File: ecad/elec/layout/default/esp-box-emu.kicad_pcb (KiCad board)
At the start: 2 copper layers, 225.7 x 100.8 mm, 25 parts

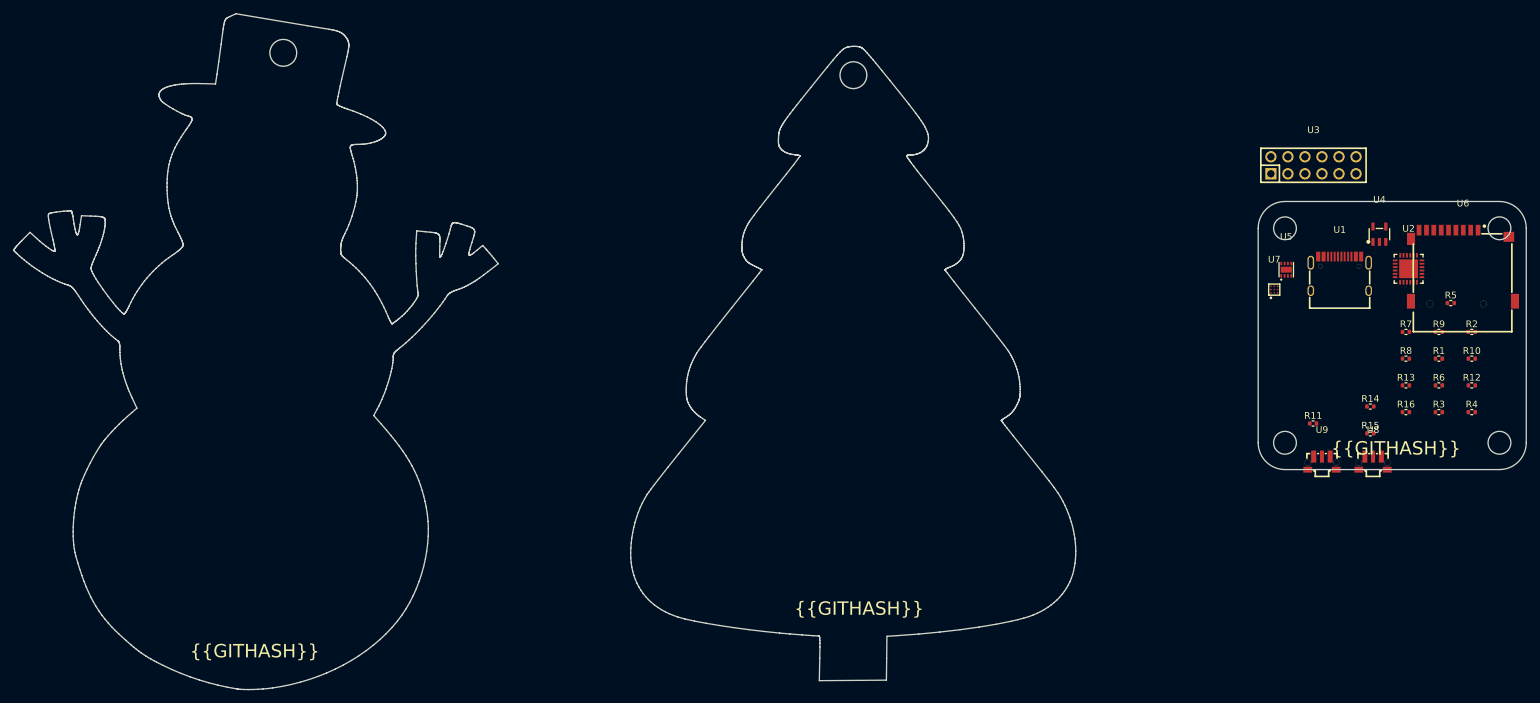
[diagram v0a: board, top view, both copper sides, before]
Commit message: playing with kicad layout for esp-box-emu board. added pmod headers
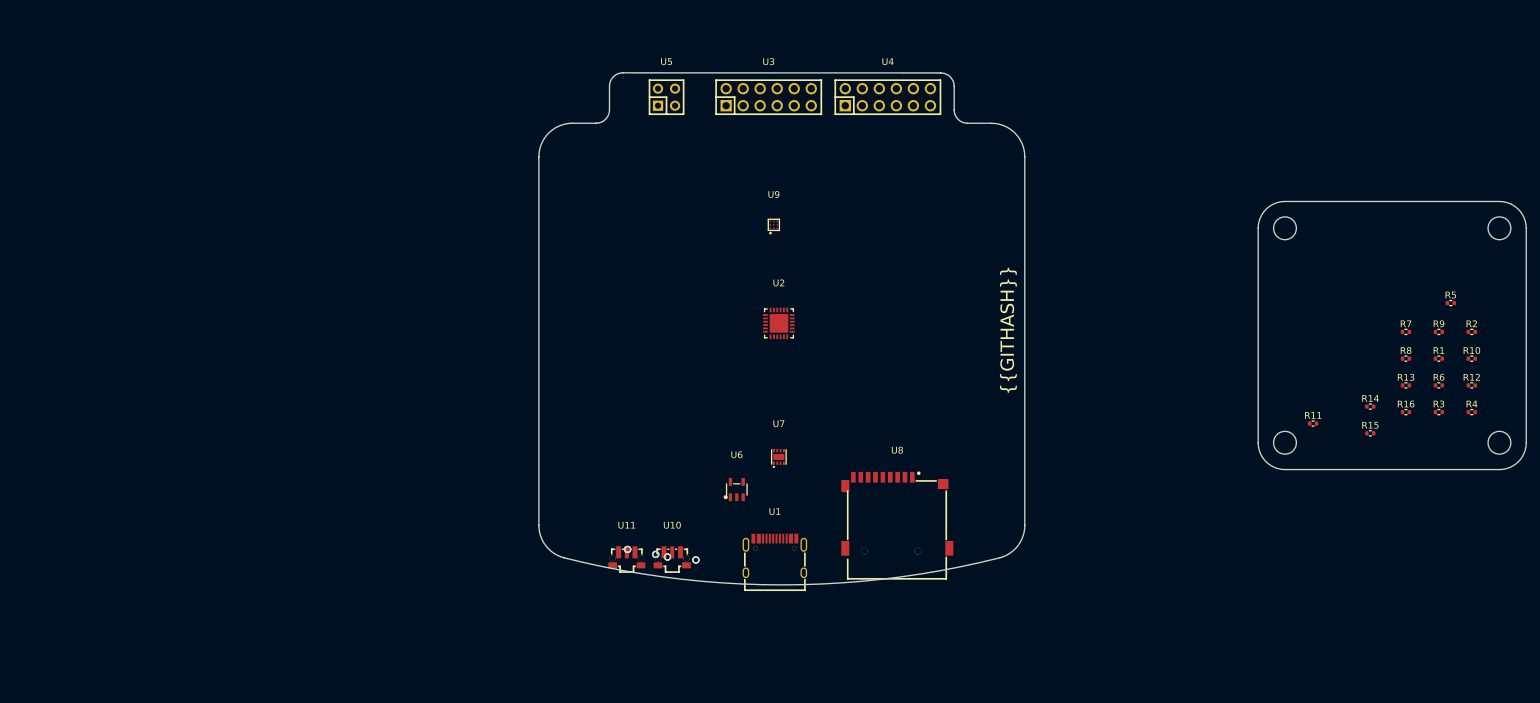
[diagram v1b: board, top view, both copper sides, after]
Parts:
- added U10: , lib:SW-SMD_E-SWITCH_TL3340, F.Cu at (134.2, 131.1)
- added U11: , lib:SW-SMD_E-SWITCH_TL3340, F.Cu at (127.4, 131.1)
- U4: footprint lib:SOT-23-5_L3.0-W1.7-P0.95-LS2.8-BL -> lib:HDR-TH_12P-P2.54-V-M-R2-C6-S2.54
- U5: footprint lib:DFN-8_L2.0-W2.0-P0.50-BL-EP -> lib:HDR-TH_4P-P2.54-V-M-R2-C2-S2.54-1
- U6: footprint lib:SIM-SMD_C9900007362 -> lib:SOT-23-5_L3.0-W1.7-P0.95-LS2.8-BL
- U7: footprint lib:DSBGA-9_L1.5-W1.5-R3-C3-P0.50-BL -> lib:DFN-8_L2.0-W2.0-P0.50-BL-EP
- U8: footprint lib:SW-SMD_E-SWITCH_TL3340 -> lib:SIM-SMD_C9900007362
- U9: footprint lib:SW-SMD_E-SWITCH_TL3340 -> lib:DSBGA-9_L1.5-W1.5-R3-C3-P0.50-BL
- moved U6 113.4 mm to (143.8, 120.8)
- moved U5 96.0 mm to (133.3, 62.2)
- moved U2 94.3 mm to (150.1, 96.0)
- moved U1 94.2 mm to (149.5, 130.6)
- moved U9 89.2 mm to (149.4, 81.3)
- moved U3 81.9 mm to (148.6, 62.2)
- moved U7 78.0 mm to (150.1, 115.9)
- moved U4 76.1 mm to (166.4, 62.2)
- moved U8 71.4 mm to (167.8, 124.2)
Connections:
- net _1 renamed pmod1-_1
- net _10 renamed pmod1-_10
- net _11 renamed pmod1-_11
- net _12 renamed pmod1-_12
- net _2 renamed pmod1-_2
- net _3 renamed pmod1-_3
- net _5 renamed pmod1-_5
- net _6 renamed pmod1-_6
- net _7 renamed pmod1-_7
- net _8 renamed pmod1-_8
- net _9 renamed pmod1-_9
- net mtp-_4 renamed pmod1-_4
- U4 pad 1: stat -> pmod2-_1
- U4 pad 2: gnd -> pmod2-_2
- U4 pad 3: vcc-2 -> pmod2-_3
- U4 pad 4: vcc-1 -> pmod2-_4
- U4 pad 5: gnd -> pmod2-_5
- U5 pad 1: ctg -> pin2x2-_1
- U5 pad 2: vcc-2 -> pin2x2-_2
- U5 pad 3: vcc-2 -> pin2x2-_3
- U5 pad 4: gnd -> pin2x2-_4
- U6 pad 1: dat2 -> stat
- U6 pad 2: cd_dat3 -> gnd
- U6 pad 3: cmd -> vcc-2
- U6 pad 4: vdd -> vcc-1
- U6 pad 5: clx -> gnd
- U8 pad 1: p1_2 -> dat2
- U8 pad 2: vcc -> cd_dat3
- U8 pad 3: vcc -> cmd
- U8 pad 4: vol_up.btn.btn-_4 -> vdd
- U8 pad 5: vol_up.btn.btn-_4 -> clx
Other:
- board size 225.7 x 100.8 mm -> 147.3 x 76.4 mm

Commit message: fleshing out more wiring and reworked pmod into separate module
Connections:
- net pmod2-_5 renamed _5
- net pmod2-_7 renamed _7
- U3 pad 10: pmod1-_10 -> gnd
- U3 pad 11: pmod1-_11 -> vcc
- U3 pad 12: pmod1-_12 -> vcc
- U3 pad 5: pmod1-_5 -> dm
- U3 pad 7: pmod1-_7 -> dp
- U3 pad 9: pmod1-_9 -> gnd
- U4 pad 10: pmod2-_10 -> gnd
- U4 pad 11: pmod2-_11 -> vcc
- U4 pad 12: pmod2-_12 -> vcc
- U4 pad 9: pmod2-_9 -> gnd
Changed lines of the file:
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@@
   (net 52 "pmod1-_3")
   (net 53 "pmod1-_4")
-  (net 54 "pmod1-_5")
-  (net 55 "pmod1-_6")
-  (net 56 "pmod1-_7")
-  (net 57 "pmod1-_8")
-  (net 58 "max17048-ep")
-  (net 59 "pin2x2-_1")
-  (net 60 "pin2x2-_2")
-  (net 61 "pin2x2-_3")
-  (net 62 "pin2x2-_4")
-  (net 63 "pmod1-_9")
-  (net 64 "pmod1-_10")
-  (net 65 "pmod1-_11")
-  (net 66 "pmod1-_12")
-  (net 67 "pmod2-_1")
-  (net 68 "pmod2-_2")
-  (net 69 "pmod2-_3")
-  (net 70 "pmod2-_4")
-  (net 71 "pmod2-_5")
-  (net 72 "pmod2-_6")
-  (net 73 "pmod2-_7")
-  (net 74 "pmod2-_8")
-  (net 75 "pmod2-_9")
-  (net 76 "pmod2-_10")
-  (net 77 "pmod2-_11")
-  (net 78 "pmod2-_12")
+  (net 54 "pmod1-_6")
+  (net 55 "pmod1-_8")
+  (net 56 "max17048-ep")
+  (net 57 "pin2x2-_1")
+  (net 58 "pin2x2-_2")
+  (net 59 "pin2x2-_3")
+  (net 60 "pin2x2-_4")
+  (net 61 "pmod2-_1")
+  (net 62 "pmod2-_2")
+  (net 63 "pmod2-_3")
+  (net 64 "pmod2-_4")
+  (net 65 "pmod2-_6")
+  (net 66 "pmod2-_8")
+  (net 67 "_5")
+  (net 68 "_7")
   (footprint "lib:SIM-SMD_C9900007362" (layer "F.Cu")
     (at 167.78 124.24)
@@
       (net 53 "pmod1-_4") (pintype "stereo"))
     (pad "5" thru_hole circle (at -1.27 1.27) (size 1.7 1.7) (drill 1.100023) (layers "*.Cu" "*.Mask")
-      (net 54 "pmod1-_5") (pintype "stereo"))
+      (net 27 "dm") (pintype "stereo"))
     (pad "6" thru_hole circle (at -1.27 -1.27) (size 1.7 1.7) (drill 1.100023) (layers "*.Cu" "*.Mask")
-      (net 55 "pmod1-_6") (pintype "stereo"))
+      (net 54 "pmod1-_6") (pintype "stereo"))
     (pad "7" thru_hole circle (at 1.27 1.27) (size 1.7 1.7) (drill 1.100023) (layers "*.Cu" "*.Mask")
-      (net 56 "pmod1-_7") (pintype "stereo"))
+      (net 28 "dp") (pintype "stereo"))
     (pad "8" thru_hole circle (at 1.27 -1.27) (size 1.7 1.7) (drill 1.100023) (layers "*.Cu" "*.Mask")
-      (net 57 "pmod1-_8") (pintype "stereo"))
+      (net 55 "pmod1-_8") (pintype "stereo"))
     (pad "9" thru_hole circle (at 3.81 1.27) (size 1.7 1.7) (drill 1.100023) (layers "*.Cu" "*.Mask")
-      (net 63 "pmod1-_9") (pintype "stereo"))
+      (net 9 "gnd") (pintype "stereo"))
     (pad "10" thru_hole circle (at 3.81 -1.27) (size 1.7 1.7) (drill 1.100023) (layers "*.Cu" "*.Mask")
-      (net 64 "pmod1-_10") (pintype "stereo"))
+      (net 9 "gnd") (pintype "stereo"))
     (pad "11" thru_hole circle (at 6.35 1.27) (size 1.7 1.7) (drill 1.100023) (layers "*.Cu" "*.Mask")
-      (net 65 "pmod1-_11") (pintype "stereo"))
+      (net 21 "vcc") (pintype "stereo"))
     (pad "12" thru_hole circle (at 6.35 -1.27) (size 1.7 1.7) (drill 1.100023) (layers "*.Cu" "*.Mask")
-      (net 66 "pmod1-_12") (pintype "stereo"))
+      (net 21 "vcc") (pintype "stereo"))
     (model "/Users/bob/esp-cpp/esp-box-emu/ecad/elec/footprints/footprints.3dshapes/HDR2.54-M-LI-2X6P.wrl"
       (offset (xyz 0 -0 0))
@@
       (stroke (width 0.06) (type solid)) (fill none) (layer "F.Fab"))
     (pad "1" thru_hole rect (at -6.35 1.27) (size 1.7 1.7) (drill 1.100023) (layers "*.Cu" "*.Mask")
-      (net 67 "pmod2-_1") (pintype "stereo"))
+      (net 61 "pmod2-_1") (pintype "stereo"))
     (pad "2" thru_hole circle (at -6.35 -1.27) (size 1.7 1.7) (drill 1.100023) (layers "*.Cu" "*.Mask")
-      (net 68 "pmod2-_2") (pintype "stereo"))
+      (net 62 "pmod2-_2") (pintype "stereo"))
     (pad "3" thru_hole circle (at -3.81 1.27) (size 1.7 1.7) (drill 1.100023) (layers "*.Cu" "*.Mask")
-      (net 69 "pmod2-_3") (pintype "stereo"))
+      (net 63 "pmod2-_3") (pintype "stereo"))
     (pad "4" thru_hole circle (at -3.81 -1.27) (size 1.7 1.7) (drill 1.100023) (layers "*.Cu" "*.Mask")
-      (net 70 "pmod2-_4") (pintype "stereo"))
+      (net 64 "pmod2-_4") (pintype "stereo"))
     (pad "5" thru_hole circle (at -1.27 1.27) (size 1.7 1.7) (drill 1.100023) (layers "*.Cu" "*.Mask")
-      (net 71 "pmod2-_5") (pintype "stereo"))
+      (net 67 "_5") (pintype "stereo"))
     (pad "6" thru_hole circle (at -1.27 -1.27) (size 1.7 1.7) (drill 1.100023) (layers "*.Cu" "*.Mask")
-      (net 72 "pmod2-_6") (pintype "stereo"))
+      (net 65 "pmod2-_6") (pintype "stereo"))
     (pad "7" thru_hole circle (at 1.27 1.27) (size 1.7 1.7) (drill 1.100023) (layers "*.Cu" "*.Mask")
-      (net 73 "pmod2-_7") (pintype "stereo"))
+      (net 68 "_7") (pintype "stereo"))
     (pad "8" thru_hole circle (at 1.27 -1.27) (size 1.7 1.7) (drill 1.100023) (layers "*.Cu" "*.Mask")
-      (net 74 "pmod2-_8") (pintype "stereo"))
+      (net 66 "pmod2-_8") (pintype "stereo"))
     (pad "9" thru_hole circle (at 3.81 1.27) (size 1.7 1.7) (drill 1.100023) (layers "*.Cu" "*.Mask")
-      (net 75 "pmod2-_9") (pintype "stereo"))
+      (net 9 "gnd") (pintype "stereo"))
     (pad "10" thru_hole circle (at 3.81 -1.27) (size 1.7 1.7) (drill 1.100023) (layers "*.Cu" "*.Mask")
-      (net 76 "pmod2-_10") (pintype "stereo"))
+      (net 9 "gnd") (pintype "stereo"))
     (pad "11" thru_hole circle (at 6.35 1.27) (size 1.7 1.7) (drill 1.100023) (layers "*.Cu" "*.Mask")
-      (net 77 "pmod2-_11") (pintype "stereo"))
+      (net 21 "vcc") (pintype "stereo"))
     (pad "12" thru_hole circle (at 6.35 -1.27) (size 1.7 1.7) (drill 1.100023) (layers "*.Cu" "*.Mask")
-      (net 78 "pmod2-_12") (pintype "stereo"))
+      (net 21 "vcc") (pintype "stereo"))
     (model "/Users/bob/esp-cpp/esp-box-emu/ecad/elec/footprints/footprints.3dshapes/HDR2.54-M-LI-2X6P.wrl"
       (offset (xyz 0 -0 0))
@@
       (net 20 "sda") (pintype "stereo"))
     (pad "9" smd rect (at 0 0) (size 1.65 0.9) (layers "F.Cu" "F.Paste" "F.Mask")
-      (net 58 "max17048-ep") (pintype "stereo"))
+      (net 56 "max17048-ep") (pintype "stereo"))
     (model "/Users/bob/esp-cpp/esp-box-emu/ecad/elec/footprints/footprints.3dshapes/DFN-8_L2.0-W2.0-H0.8-P0.50.wrl"
       (offset (xyz 0 -0 -0))
@@
       (stroke (width 0.06) (type solid)) (fill none) (layer "F.Fab"))
     (pad "1" thru_hole rect (at -1.27 1.27) (size 1.52 1.52) (drill 0.9144) (layers "*.Cu" "*.Mask")
-      (net 59 "pin2x2-_1") (pintype "stereo"))
+      (net 57 "pin2x2-_1") (pintype "stereo"))
     (pad "2" thru_hole circle (at -1.27 -1.27) (size 1.52 1.52) (drill 0.9144) (layers "*.Cu" "*.Mask")
-      (net 60 "pin2x2-_2") (pintype "stereo"))
+      (net 58 "pin2x2-_2") (pintype "stereo"))
     (pad "3" thru_hole circle (at 1.27 1.27) (size 1.52 1.52) (drill 0.9144) (layers "*.Cu" "*.Mask")
-      (net 61 "pin2x2-_3") (pintype "stereo"))
+      (net 59 "pin2x2-_3") (pintype "stereo"))
     (pad "4" thru_hole circle (at 1.27 -1.27) (size 1.52 1.52) (drill 0.9144) (layers "*.Cu" "*.Mask")
-      (net 62 "pin2x2-_4") (pintype "stereo"))
+      (net 60 "pin2x2-_4") (pintype "stereo"))
     (model "/Users/bob/esp-cpp/esp-box-emu/ecad/elec/footprints/footprints.3dshapes/HDR2.54-M-LI-2x2P.wrl"
       (offset (xyz 0 -0 0))

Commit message: fleshing out uSD card
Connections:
- net cd_dat3 renamed dat3
- net clx renamed clk
- net uSD-ep renamed uSD.card-ep
- U8 pad 4: vdd -> vcc
- U8 pad 6: vss -> gnd
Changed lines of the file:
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@@
   (net 39 "sbu1")
   (net 40 "dat2")
-  (net 41 "cd_dat3")
-  (net 42 "cmd")
-  (net 43 "vdd")
-  (net 44 "clx")
-  (net 45 "vss")
-  (net 46 "dat0")
-  (net 47 "dat1")
-  (net 48 "net")
-  (net 49 "uSD-ep")
-  (net 50 "pmod1-_1")
-  (net 51 "pmod1-_2")
-  (net 52 "pmod1-_3")
-  (net 53 "pmod1-_4")
-  (net 54 "pmod1-_6")
-  (net 55 "pmod1-_8")
-  (net 56 "max17048-ep")
-  (net 57 "pin2x2-_1")
-  (net 58 "pin2x2-_2")
-  (net 59 "pin2x2-_3")
-  (net 60 "pin2x2-_4")
-  (net 61 "pmod2-_1")
-  (net 62 "pmod2-_2")
-  (net 63 "pmod2-_3")
-  (net 64 "pmod2-_4")
-  (net 65 "pmod2-_6")
-  (net 66 "pmod2-_8")
-  (net 67 "_5")
-  (net 68 "_7")
+  (net 41 "cmd")
+  (net 42 "dat0")
+  (net 43 "dat1")
+  (net 44 "net")
+  (net 45 "pmod1-_1")
+  (net 46 "pmod1-_2")
+  (net 47 "pmod1-_3")
+  (net 48 "pmod1-_4")
+  (net 49 "pmod1-_6")
+  (net 50 "pmod1-_8")
+  (net 51 "max17048-ep")
+  (net 52 "pin2x2-_1")
+  (net 53 "pin2x2-_2")
+  (net 54 "pin2x2-_3")
+  (net 55 "pin2x2-_4")
+  (net 56 "pmod2-_1")
+  (net 57 "pmod2-_2")
+  (net 58 "pmod2-_3")
+  (net 59 "pmod2-_4")
+  (net 60 "pmod2-_6")
+  (net 61 "pmod2-_8")
+  (net 62 "_5")
+  (net 63 "_7")
+  (net 64 "dat3")
+  (net 65 "clk")
+  (net 66 "uSD.card-ep")
   (footprint "lib:SIM-SMD_C9900007362" (layer "F.Cu")
     (at 167.78 124.24)
@@
       (net 40 "dat2") (pintype "stereo"))
     (pad "2" smd rect (at 1.15 -5.3) (size 0.7 1.6) (layers "F.Cu" "F.Paste" "F.Mask")
-      (net 41 "cd_dat3") (pintype "stereo"))
+      (net 64 "dat3") (pintype "stereo"))
     (pad "3" smd rect (at 0.05 -5.3) (size 0.7 1.6) (layers "F.Cu" "F.Paste" "F.Mask")
-      (net 42 "cmd") (pintype "stereo"))
+      (net 41 "cmd") (pintype "stereo"))
     (pad "4" smd rect (at -1.05 -5.3) (size 0.7 1.6) (layers "F.Cu" "F.Paste" "F.Mask")
-      (net 43 "vdd") (pintype "stereo"))
+      (net 21 "vcc") (pintype "stereo"))
     (pad "5" smd rect (at -2.15 -5.3) (size 0.7 1.6) (layers "F.Cu" "F.Paste" "F.Mask")
-      (net 44 "clx") (pintype "stereo"))
+      (net 65 "clk") (pintype "stereo"))
     (pad "6" smd rect (at -3.25 -5.3) (size 0.7 1.6) (layers "F.Cu" "F.Paste" "F.Mask")
-      (net 45 "vss") (pintype "stereo"))
+      (net 9 "gnd") (pintype "stereo"))
     (pad "7" smd rect (at -4.35 -5.3) (size 0.7 1.6) (layers "F.Cu" "F.Paste" "F.Mask")
-      (net 46 "dat0") (pintype "stereo"))
+      (net 42 "dat0") (pintype "stereo"))
     (pad "8" smd rect (at -5.45 -5.3) (size 0.7 1.6) (layers "F.Cu" "F.Paste" "F.Mask")
-      (net 47 "dat1") (pintype "stereo"))
+      (net 43 "dat1") (pintype "stereo"))
     (pad "CD" smd rect (at -6.55 -5.3) (size 0.7 1.6) (layers "F.Cu" "F.Paste" "F.Mask")
-      (net 48 "net") (pintype "stereo"))
+      (net 44 "net") (pintype "stereo"))
     (pad "G" smd rect (at -7.76 5.3) (size 1.2 2.2) (layers "F.Cu" "F.Paste" "F.Mask")
-      (net 49 "uSD-ep") (pintype "stereo"))
+      (net 66 "uSD.card-ep") (pintype "stereo"))
     (pad "G" smd rect (at -7.75 -3.99) (size 1.2 1.8) (layers "F.Cu" "F.Paste" "F.Mask")
-      (net 49 "uSD-ep") (pintype "stereo"))
+      (net 66 "uSD.card-ep") (pintype "stereo"))
     (pad "G" smd rect (at 6.85 -4.29) (size 1.6 1.5) (layers "F.Cu" "F.Paste" "F.Mask")
-      (net 49 "uSD-ep") (pintype "stereo"))
+      (net 66 "uSD.card-ep") (pintype "stereo"))
     (pad "G" smd rect (at 7.76 5.3) (size 1.2 2.2) (layers "F.Cu" "F.Paste" "F.Mask")
-      (net 49 "uSD-ep") (pintype "stereo"))
+      (net 66 "uSD.card-ep") (pintype "stereo"))
     (model "/Users/bob/esp-cpp/esp-box-emu/ecad/elec/footprints/footprints.3dshapes/SIM-SMD_C9900007362.wrl"
       (offset (xyz -0 -2.19 0.5))
@@
       (stroke (width 0.06) (type solid)) (fill none) (layer "F.Fab"))
     (pad "1" thru_hole rect (at -6.35 1.27) (size 1.7 1.7) (drill 1.100023) (layers "*.Cu" "*.Mask")
-      (net 50 "pmod1-_1") (pintype "stereo"))
+      (net 45 "pmod1-_1") (pintype "stereo"))
     (pad "2" thru_hole circle (at -6.35 -1.27) (size 1.7 1.7) (drill 1.100023) (layers "*.Cu" "*.Mask")
-      (net 51 "pmod1-_2") (pintype "stereo"))
+      (net 46 "pmod1-_2") (pintype "stereo"))
     (pad "3" thru_hole circle (at -3.81 1.27) (size 1.7 1.7) (drill 1.100023) (layers "*.Cu" "*.Mask")
-      (net 52 "pmod1-_3") (pintype "stereo"))
+      (net 47 "pmod1-_3") (pintype "stereo"))
     (pad "4" thru_hole circle (at -3.81 -1.27) (size 1.7 1.7) (drill 1.100023) (layers "*.Cu" "*.Mask")
-      (net 53 "pmod1-_4") (pintype "stereo"))
+      (net 48 "pmod1-_4") (pintype "stereo"))
     (pad "5" thru_hole circle (at -1.27 1.27) (size 1.7 1.7) (drill 1.100023) (layers "*.Cu" "*.Mask")
       (net 27 "dm") (pintype "stereo"))
     (pad "6" thru_hole circle (at -1.27 -1.27) (size 1.7 1.7) (drill 1.100023) (layers "*.Cu" "*.Mask")
-      (net 54 "pmod1-_6") (pintype "stereo"))
+      (net 49 "pmod1-_6") (pintype "stereo"))
     (pad "7" thru_hole circle (at 1.27 1.27) (size 1.7 1.7) (drill 1.100023) (layers "*.Cu" "*.Mask")
       (net 28 "dp") (pintype "stereo"))
     (pad "8" thru_hole circle (at 1.27 -1.27) (size 1.7 1.7) (drill 1.100023) (layers "*.Cu" "*.Mask")
-      (net 55 "pmod1-_8") (pintype "stereo"))
+      (net 50 "pmod1-_8") (pintype "stereo"))
     (pad "9" thru_hole circle (at 3.81 1.27) (size 1.7 1.7) (drill 1.100023) (layers "*.Cu" "*.Mask")
       (net 9 "gnd") (pintype "stereo"))
@@
       (stroke (width 0.06) (type solid)) (fill none) (layer "F.Fab"))
     (pad "1" thru_hole rect (at -6.35 1.27) (size 1.7 1.7) (drill 1.100023) (layers "*.Cu" "*.Mask")
-      (net 61 "pmod2-_1") (pintype "stereo"))
+      (net 56 "pmod2-_1") (pintype "stereo"))
     (pad "2" thru_hole circle (at -6.35 -1.27) (size 1.7 1.7) (drill 1.100023) (layers "*.Cu" "*.Mask")
-      (net 62 "pmod2-_2") (pintype "stereo"))
+      (net 57 "pmod2-_2") (pintype "stereo"))
     (pad "3" thru_hole circle (at -3.81 1.27) (size 1.7 1.7) (drill 1.100023) (layers "*.Cu" "*.Mask")
-      (net 63 "pmod2-_3") (pintype "stereo"))
+      (net 58 "pmod2-_3") (pintype "stereo"))
     (pad "4" thru_hole circle (at -3.81 -1.27) (size 1.7 1.7) (drill 1.100023) (layers "*.Cu" "*.Mask")
-      (net 64 "pmod2-_4") (pintype "stereo"))
+      (net 59 "pmod2-_4") (pintype "stereo"))
     (pad "5" thru_hole circle (at -1.27 1.27) (size 1.7 1.7) (drill 1.100023) (layers "*.Cu" "*.Mask")
-      (net 67 "_5") (pintype "stereo"))
+      (net 62 "_5") (pintype "stereo"))
     (pad "6" thru_hole circle (at -1.27 -1.27) (size 1.7 1.7) (drill 1.100023) (layers "*.Cu" "*.Mask")
-      (net 65 "pmod2-_6") (pintype "stereo"))
+      (net 60 "pmod2-_6") (pintype "stereo"))
     (pad "7" thru_hole circle (at 1.27 1.27) (size 1.7 1.7) (drill 1.100023) (layers "*.Cu" "*.Mask")
-      (net 68 "_7") (pintype "stereo"))
+      (net 63 "_7") (pintype "stereo"))
     (pad "8" thru_hole circle (at 1.27 -1.27) (size 1.7 1.7) (drill 1.100023) (layers "*.Cu" "*.Mask")
-      (net 66 "pmod2-_8") (pintype "stereo"))
+      (net 61 "pmod2-_8") (pintype "stereo"))
     (pad "9" thru_hole circle (at 3.81 1.27) (size 1.7 1.7) (drill 1.100023) (layers "*.Cu" "*.Mask")
       (net 9 "gnd") (pintype "stereo"))
@@
       (net 20 "sda") (pintype "stereo"))
     (pad "9" smd rect (at 0 0) (size 1.65 0.9) (layers "F.Cu" "F.Paste" "F.Mask")
-      (net 56 "max17048-ep") (pintype "stereo"))
+      (net 51 "max17048-ep") (pintype "stereo"))
     (model "/Users/bob/esp-cpp/esp-box-emu/ecad/elec/footprints/footprints.3dshapes/DFN-8_L2.0-W2.0-H0.8-P0.50.wrl"
       (offset (xyz 0 -0 -0))
@@
       (stroke (width 0.06) (type solid)) (fill none) (layer "F.Fab"))
     (pad "1" thru_hole rect (at -1.27 1.27) (size 1.52 1.52) (drill 0.9144) (layers "*.Cu" "*.Mask")
-      (net 57 "pin2x2-_1") (pintype "stereo"))
+      (net 52 "pin2x2-_1") (pintype "stereo"))
     (pad "2" thru_hole circle (at -1.27 -1.27) (size 1.52 1.52) (drill 0.9144) (layers "*.Cu" "*.Mask")
-      (net 58 "pin2x2-_2") (pintype "stereo"))
+      (net 53 "pin2x2-_2") (pintype "stereo"))
     (pad "3" thru_hole circle (at 1.27 1.27) (size 1.52 1.52) (drill 0.9144) (layers "*.Cu" "*.Mask")
-      (net 59 "pin2x2-_3") (pintype "stereo"))
+      (net 54 "pin2x2-_3") (pintype "stereo"))
     (pad "4" thru_hole circle (at 1.27 -1.27) (size 1.52 1.52) (drill 0.9144) (layers "*.Cu" "*.Mask")
-      (net 60 "pin2x2-_4") (pintype "stereo"))
+      (net 55 "pin2x2-_4") (pintype "stereo"))
     (model "/Users/bob/esp-cpp/esp-box-emu/ecad/elec/footprints/footprints.3dshapes/HDR2.54-M-LI-2x2P.wrl"
       (offset (xyz 0 -0 0))
